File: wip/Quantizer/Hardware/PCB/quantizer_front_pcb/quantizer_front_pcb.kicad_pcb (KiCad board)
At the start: 2 copper layers, 40 x 100 mm, 38 parts, among them J1 THONKICONN, J13 Conn_01x12_Female, J14 Conn_01x04_Female, J15 Conn_01x04_Female, J16 Conn_01x02_Female, J2 THONKICONN, J3 THONKICONN, J4 THONKICONN, J5 THONKICONN, J6 THONKICONN

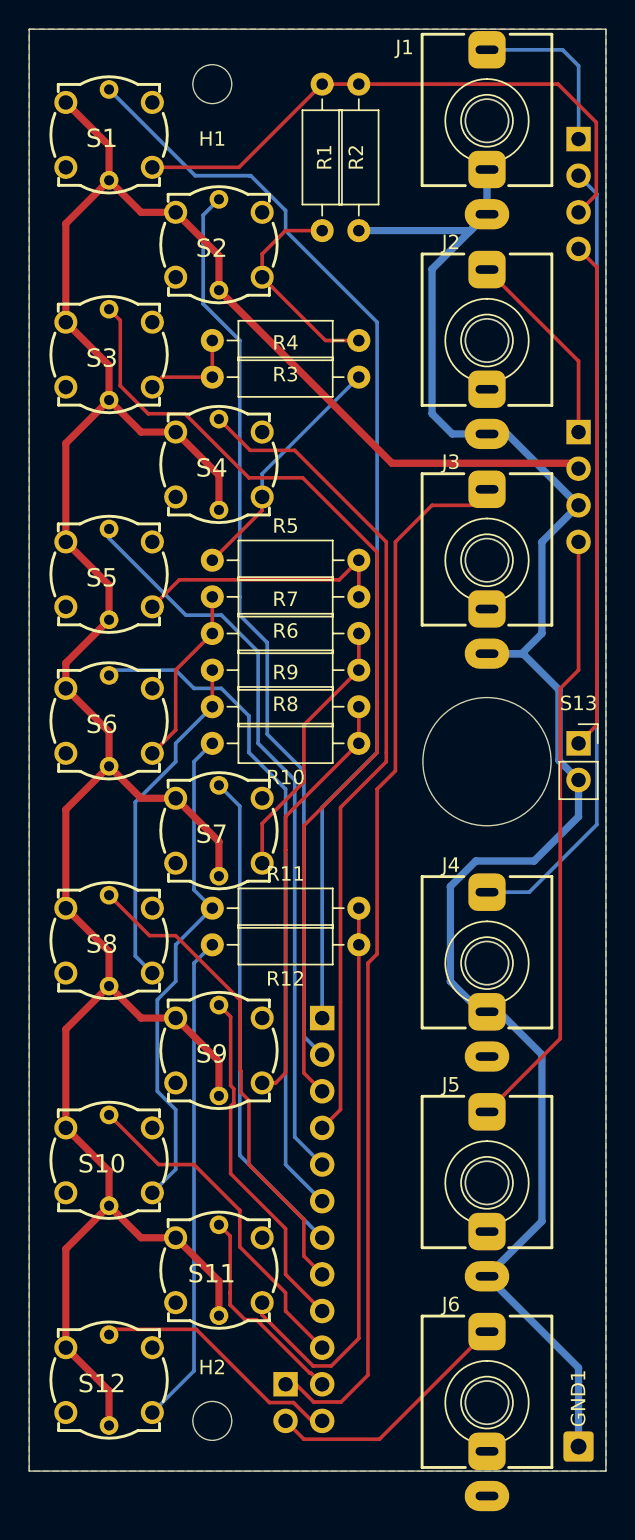
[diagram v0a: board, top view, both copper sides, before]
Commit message: fixed quantizer
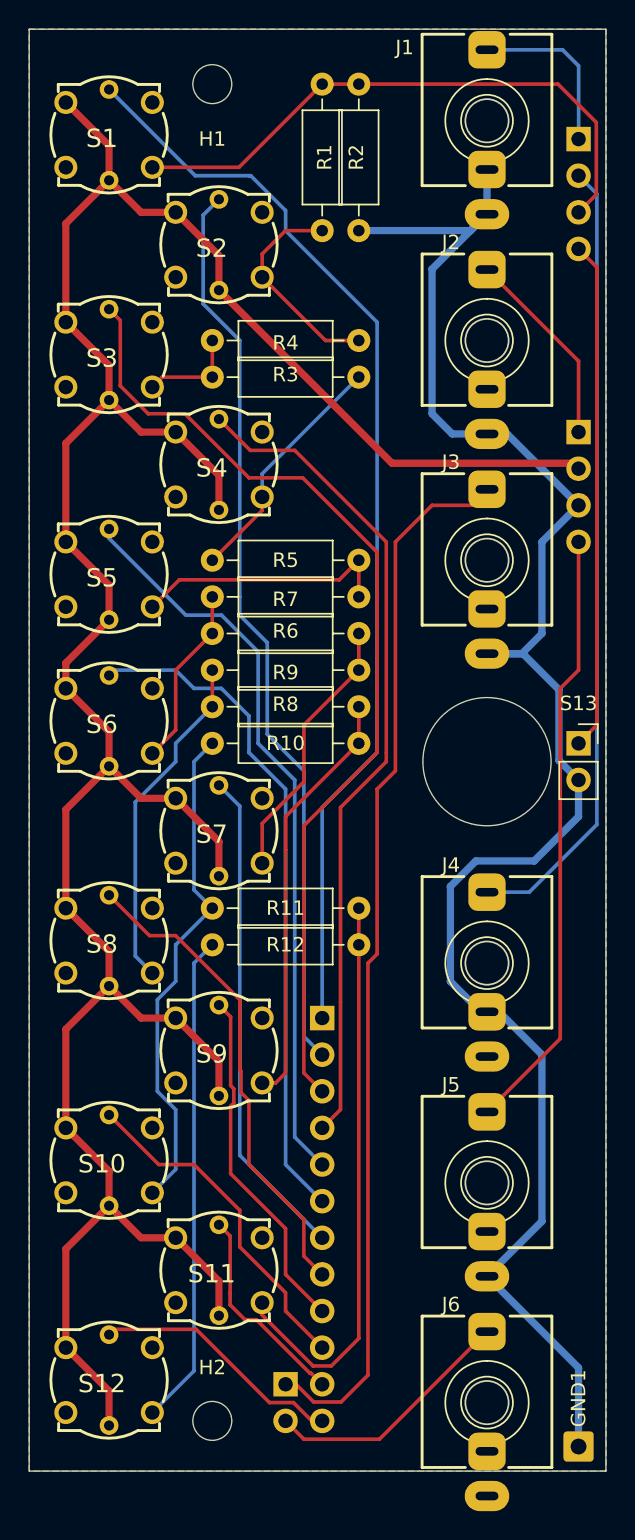
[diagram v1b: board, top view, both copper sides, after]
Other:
- board text added: "quantizer_front_v0.4"
- board text removed: "quantizer_front_v0.3"
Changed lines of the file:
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@@
     (47 F.CrtYd user)
     (48 B.Fab user)
-    (49 F.Fab user)
+    (49 F.Fab user hide)
   )
   (setup
@@
     (pcbplotparams
       (layerselection 0x010fc_ffffffff)
-      (usegerberextensions false)
-      (usegerberattributes true)
-      (usegerberadvancedattributes true)
-      (creategerberjobfile true)
+      (usegerberextensions true)
+      (usegerberattributes false)
+      (usegerberadvancedattributes false)
+      (creategerberjobfile false)
       (excludeedgelayer true)
       (linewidth 0.100000)
@@
       (effects (font (size 0.52 0.52) (thickness 0.08)))
     )
-    (pad 1 thru_hole roundrect (at 0 0) (size 2.1 2.1) (drill 1.1) (layers *.Cu *.Mask) (roundrect_rratio 0.119047619047619)
+    (pad 1 thru_hole roundrect (at 0 0) (size 2.1 2.1) (drill 1.1) (layers *.Cu *.Mask) (roundrect_rratio 0.1190471428571429)
       (net 2 GND))
     (model ${KISYS3DMOD}/Connector_Wire.3dshapes/SolderWire-0.5sqmm_1x01_D0.9mm_OD2.1mm.wrl
@@
     (descr "Resistor, Axial_DIN0207 series, Axial, Horizontal, pin pitch=10.16mm, 0.25W = 1/4W, length*diameter=6.3*2.5mm^2, http://cdn-reichelt.de/documents/datenblatt/B400/1_4W%23YAG.pdf")
     (tags "Resistor Axial_DIN0207 series Axial Horizontal pin pitch 10.16mm 0.25W = 1/4W length 6.3mm diameter 2.5mm")
-    (fp_text reference R12 (at 5.08 -2.37) (layer F.SilkS)
+    (fp_text reference R12 (at 5.08 0) (layer F.SilkS)
       (effects (font (size 1 1) (thickness 0.15)))
     )
@@
     (descr "Resistor, Axial_DIN0207 series, Axial, Horizontal, pin pitch=10.16mm, 0.25W = 1/4W, length*diameter=6.3*2.5mm^2, http://cdn-reichelt.de/documents/datenblatt/B400/1_4W%23YAG.pdf")
     (tags "Resistor Axial_DIN0207 series Axial Horizontal pin pitch 10.16mm 0.25W = 1/4W length 6.3mm diameter 2.5mm")
-    (fp_text reference R11 (at 5.08 -2.37) (layer F.SilkS)
+    (fp_text reference R11 (at 5.08 0) (layer F.SilkS)
       (effects (font (size 1 1) (thickness 0.15)))
     )
@@
     (descr "Resistor, Axial_DIN0207 series, Axial, Horizontal, pin pitch=10.16mm, 0.25W = 1/4W, length*diameter=6.3*2.5mm^2, http://cdn-reichelt.de/documents/datenblatt/B400/1_4W%23YAG.pdf")
     (tags "Resistor Axial_DIN0207 series Axial Horizontal pin pitch 10.16mm 0.25W = 1/4W length 6.3mm diameter 2.5mm")
-    (fp_text reference R10 (at 5.08 -2.37) (layer F.SilkS)
+    (fp_text reference R10 (at 5.08 0) (layer F.SilkS)
       (effects (font (size 1 1) (thickness 0.15)))
     )
@@
     (descr "Resistor, Axial_DIN0207 series, Axial, Horizontal, pin pitch=10.16mm, 0.25W = 1/4W, length*diameter=6.3*2.5mm^2, http://cdn-reichelt.de/documents/datenblatt/B400/1_4W%23YAG.pdf")
     (tags "Resistor Axial_DIN0207 series Axial Horizontal pin pitch 10.16mm 0.25W = 1/4W length 6.3mm diameter 2.5mm")
-    (fp_text reference R5 (at 5.08 -2.37) (layer F.SilkS)
+    (fp_text reference R5 (at 5.08 0) (layer F.SilkS)
       (effects (font (size 1 1) (thickness 0.15)))
     )
@@
     )
   )
-  (gr_text quantizer_front_v0.3 (at 59.055 97.155 -90) (layer B.SilkS)
+  (gr_text quantizer_front_v0.4 (at 59.055 97.155 -90) (layer B.SilkS)
     (effects (font (size 0.762 0.762) (thickness 0.127)) (justify mirror))
   )
